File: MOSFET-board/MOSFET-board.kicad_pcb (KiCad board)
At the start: 2 copper layers, 63.5 x 63.5 mm, 104 parts, among them J1 PCIE-LP-01-01-F-DV-A-TR, J2 DB25_Female, U1 BTS3080EJXUMA1, U10 BTS3080EJXUMA1, U11 PCF8575_Breakout, U2 BTS3080EJXUMA1, U3 BTS3080EJXUMA1, U4 BTS3080EJXUMA1, U5 BTS3080EJXUMA1, U6 BTS3080EJXUMA1, U7 BTS3080EJXUMA1, U8 BTS3080EJXUMA1, U9 BTS3080EJXUMA1

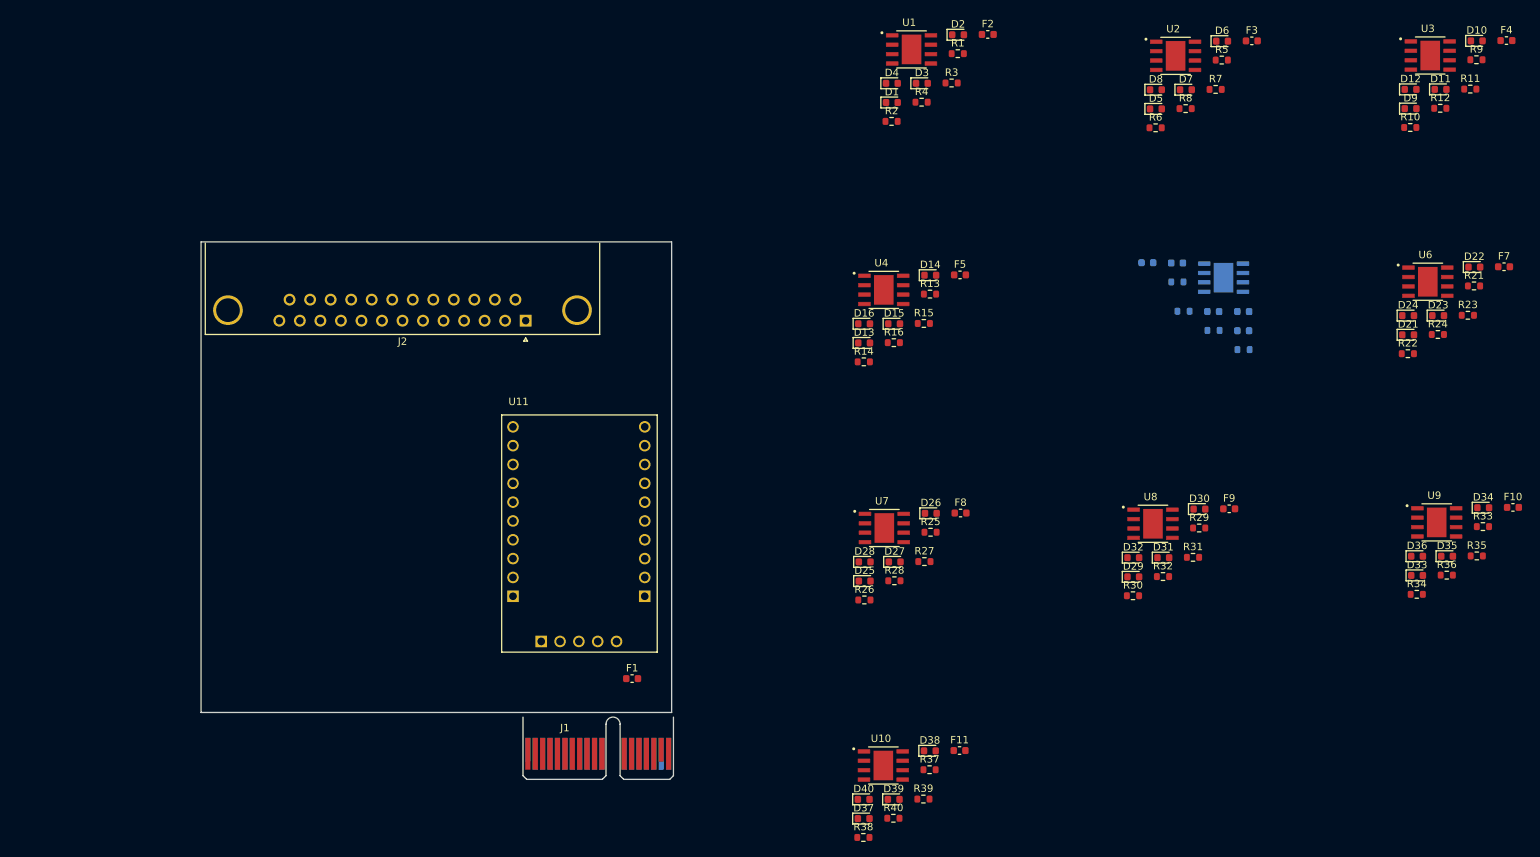
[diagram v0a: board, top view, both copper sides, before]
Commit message: Basic routing for MOSFET board. Need silkscreen update.
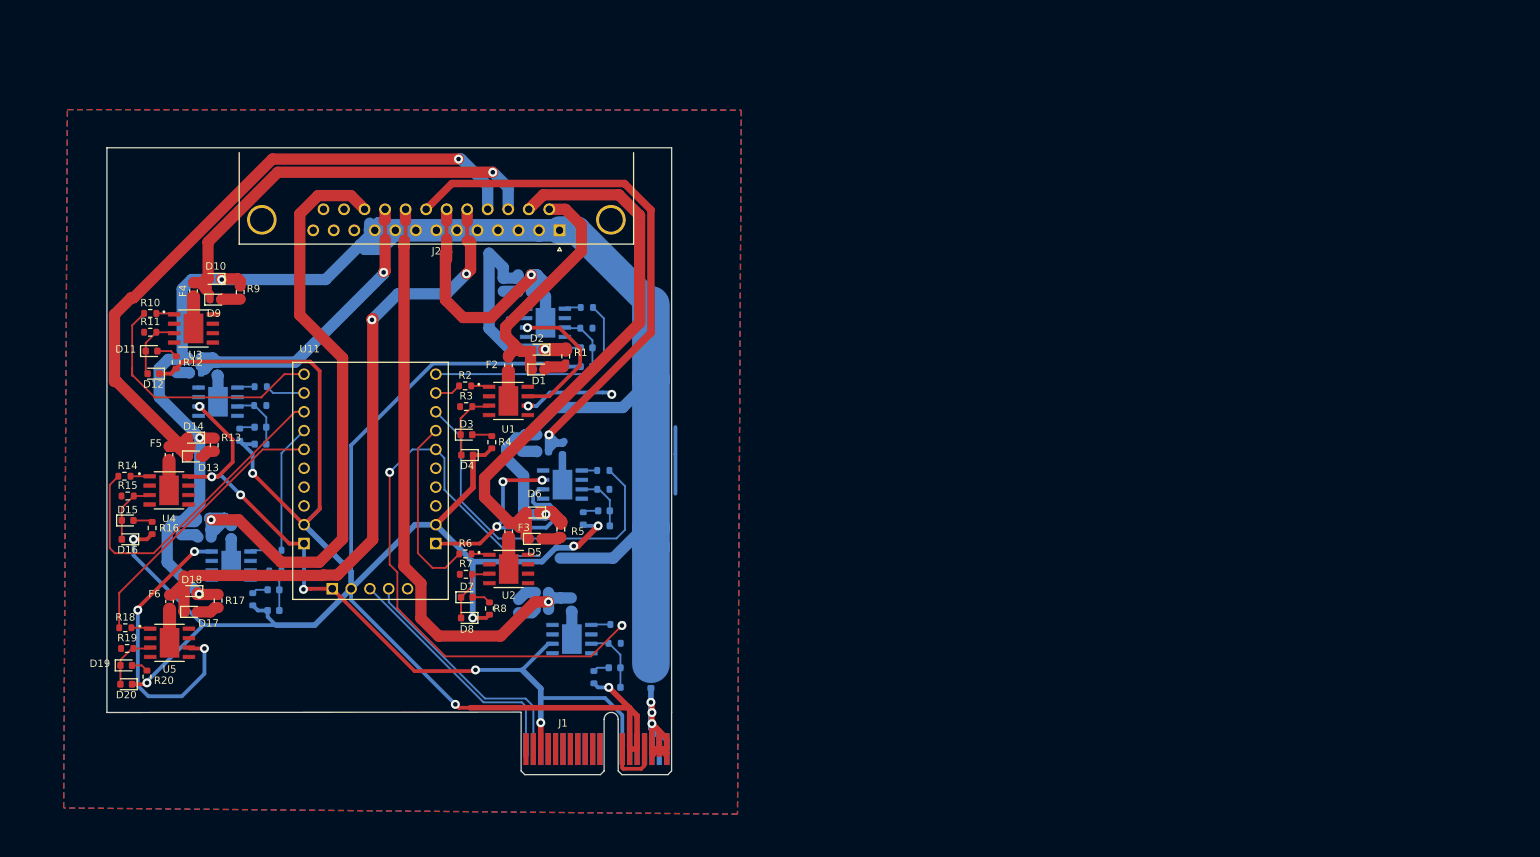
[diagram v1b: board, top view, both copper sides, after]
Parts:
- D17, D18, D19, D20, F6, R17, R18, R19, R20, U5: moved to F.Cu
- D21, D22, D23, D24, D25, D26, D27, D28, D29, D30, D31, D32, D33, D34, D35, D36, D37, D38, D39, D40, F1, F10, F11, F7, F8, F9, R21, R22, R23, R24, R25, R26, R27, R28, R29, R30, R31, R32, R33, R34, R35, R36, R37, R38, R39, R40, U10, U6, U7, U8, U9: moved to B.Cu
- moved R11 181.1 mm to (132.8, 88.4)
- moved F4 180.4 mm to (138.7, 82.8), turned to 90 degrees
- moved R33 177.6 mm to (136.4, 92.9), turned to -90 degrees
- moved D11 177.5 mm to (133.0, 90.9)
- moved F10 175.9 mm to (141.8, 93.2), turned to 90 degrees
- moved D34 175.0 mm to (138.9, 91.9)
- moved R12 174.0 mm to (136.3, 92.5), turned to -90 degrees
- moved D12 173.9 mm to (133.3, 94.0), turned to 180 degrees
- moved D10 173.4 mm to (141.4, 81.2), turned to 180 degrees
- moved R10 171.9 mm to (132.8, 85.9)
- moved U3 170.9 mm to (138.7, 87.9)
- moved R9 169.7 mm to (145.0, 83.0), turned to -90 degrees
- moved D33 167.1 mm to (138.9, 93.9), turned to 180 degrees
- moved R35 165.4 mm to (147.7, 98.3), turned to 180 degrees
- moved U9 165.3 mm to (142.0, 97.8), turned to 180 degrees
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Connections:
- D10 pad 1: Net-(D10-Pad1) -> +12V
- D12 pad 2: PYRO3ST -> Net-(D11-Pad1)
- D14 pad 1: Net-(D14-Pad1) -> +12V
- D16 pad 2: PYRO4ST -> Net-(D15-Pad1)
- D18 pad 1: Net-(D18-Pad1) -> +12V
- D2 pad 1: Net-(D2-Pad1) -> +12V
- D20 pad 2: PYRO5ST -> Net-(D19-Pad1)
- D22 pad 1: Net-(D22-Pad1) -> +12V
- D24 pad 2: PYRO6ST -> Net-(D23-Pad1)
- D26 pad 1: Net-(D26-Pad1) -> +12V
- D28 pad 2: PYRO7ST -> Net-(D27-Pad1)
- D30 pad 1: Net-(D30-Pad1) -> +12V
- D32 pad 2: PYRO8ST -> Net-(D31-Pad1)
- D34 pad 1: Net-(D34-Pad1) -> +12V
- D36 pad 2: PYRO9ST -> Net-(D35-Pad1)
- D38 pad 1: Net-(D38-Pad1) -> +12V
- D4 pad 2: PYRO1ST -> Net-(D3-Pad1)
- D40 pad 2: PYRO10ST -> Net-(D39-Pad1)
- D6 pad 1: Net-(D6-Pad1) -> +12V
- D8 pad 2: PYRO2ST -> Net-(D7-Pad1)
- F10 pad 1: +12V -> Net-(F10-Pad1)
- F10 pad 2: Net-(D34-Pad1) -> PYRO9
- F11 pad 1: +12V -> Net-(F11-Pad1)
- F11 pad 2: Net-(D38-Pad1) -> PYRO10
- F2 pad 1: +12V -> Net-(F2-Pad1)
- F2 pad 2: Net-(D2-Pad1) -> PYRO1
- F3 pad 1: +12V -> Net-(F3-Pad1)
- F3 pad 2: Net-(D6-Pad1) -> PYRO2
- F4 pad 1: +12V -> Net-(F4-Pad1)
- F4 pad 2: Net-(D10-Pad1) -> PYRO3
- F5 pad 1: +12V -> Net-(F5-Pad1)
- F5 pad 2: Net-(D14-Pad1) -> PYRO4
- F6 pad 1: +12V -> Net-(F6-Pad1)
- F6 pad 2: Net-(D18-Pad1) -> PYRO5
- F7 pad 1: +12V -> Net-(F7-Pad1)
- F7 pad 2: Net-(D22-Pad1) -> PYRO6
- F8 pad 1: +12V -> Net-(F8-Pad1)
- F8 pad 2: Net-(D26-Pad1) -> PYRO7
- F9 pad 1: +12V -> Net-(F9-Pad1)
- F9 pad 2: Net-(D30-Pad1) -> PYRO8
- R1 pad 1: Net-(D2-Pad1) -> +12V
- R11 pad 1: PYRO3ST -> /Pyro 3/Status
- R13 pad 1: Net-(D14-Pad1) -> +12V
- R15 pad 1: PYRO4ST -> /Pyro 4/Status
- R17 pad 1: Net-(D18-Pad1) -> +12V
- R19 pad 1: PYRO5ST -> /Pyro 5/Status
- R21 pad 1: Net-(D22-Pad1) -> +12V
- R23 pad 1: PYRO6ST -> /Pyro 6/Status
- R25 pad 1: Net-(D26-Pad1) -> +12V
- R27 pad 1: PYRO7ST -> /Pyro 7/Status
- R29 pad 1: Net-(D30-Pad1) -> +12V
- R3 pad 1: PYRO1ST -> /Pyro 1/Status
- R31 pad 1: PYRO8ST -> /Pyro 8/Status
- R33 pad 1: Net-(D34-Pad1) -> +12V
- R35 pad 1: PYRO9ST -> /Pyro 9/Status
- R37 pad 1: Net-(D38-Pad1) -> +12V
- R39 pad 1: PYRO10ST -> /Pyro 10/Status
- R5 pad 1: Net-(D6-Pad1) -> +12V
- R7 pad 1: PYRO2ST -> /Pyro 2/Status
- R9 pad 1: Net-(D10-Pad1) -> +12V
- U1 pad 9: PYRO1 -> Net-(F2-Pad1)
- U10 pad 9: PYRO10 -> Net-(F11-Pad1)
- U11 pad 1: PYRO9EN -> PYRO3EN
- U11 pad 18: PYRO1EN -> unconnected-(U11-Pad18)
- U11 pad 19: PYRO2EN -> unconnected-(U11-Pad19)
- U11 pad 2: PYRO10EN -> PYRO9EN
- U11 pad 20: PYRO3EN -> unconnected-(U11-Pad20)
- U11 pad 21: PYRO4EN -> PYRO8EN
- U11 pad 22: PYRO5EN -> PYRO2EN
- U11 pad 23: PYRO6EN -> PYRO7EN
- U11 pad 24: PYRO7EN -> PYRO1EN
- U11 pad 25: PYRO8EN -> PYRO6EN
- U11 pad 3: unconnected-(U11-Pad3) -> PYRO4EN
- U11 pad 4: unconnected-(U11-Pad4) -> PYRO10EN
- U11 pad 5: unconnected-(U11-Pad5) -> PYRO5EN
- U2 pad 9: PYRO2 -> Net-(F3-Pad1)
- U3 pad 9: PYRO3 -> Net-(F4-Pad1)
- U4 pad 9: PYRO4 -> Net-(F5-Pad1)
- U5 pad 9: PYRO5 -> Net-(F6-Pad1)
- U6 pad 9: PYRO6 -> Net-(F7-Pad1)
- U7 pad 9: PYRO7 -> Net-(F8-Pad1)
- U8 pad 9: PYRO8 -> Net-(F9-Pad1)
- U9 pad 9: PYRO9 -> Net-(F10-Pad1)
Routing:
- net +3.3V: track 0.00 -> 320.8 mm, vias 0 -> 8
- net +12V: track 0.00 -> 283.2 mm, vias 0 -> 5
- net GND: track 0.00 -> 223.7 mm, vias 0 -> 15
- net PYRO4: track 0.00 -> 92.8 mm, vias 0 -> 1
- net PYRO5: track 0.00 -> 90.0 mm, vias 0 -> 2
- net PYRO10: track 0.00 -> 86.8 mm, vias 0 -> 1
- net PYRO8: track 0.00 -> 83.9 mm, vias 0 -> 1
- net PYRO8EN: track 0.00 -> 83.7 mm, vias 0 -> 2
- net PYRO2: track 0.00 -> 76.2 mm
- net PYRO7: track 0.00 -> 75.7 mm, vias 0 -> 1
- net PYRO3: track 0.00 -> 59.5 mm, vias 0 -> 1
- net PYRO7EN: track 0.00 -> 47.0 mm
- net PYRO9: track 0.00 -> 44.7 mm, vias 0 -> 1
- net PYRO4EN: track 0.00 -> 44.6 mm
- net PYRO6: track 0.00 -> 39.6 mm, vias 0 -> 1
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- added copper zone on B.Cu, net GND
- added copper zone on F.Cu, net GND
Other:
- board size 63.5 x 63.5 mm -> 76.2 x 76.2 mm

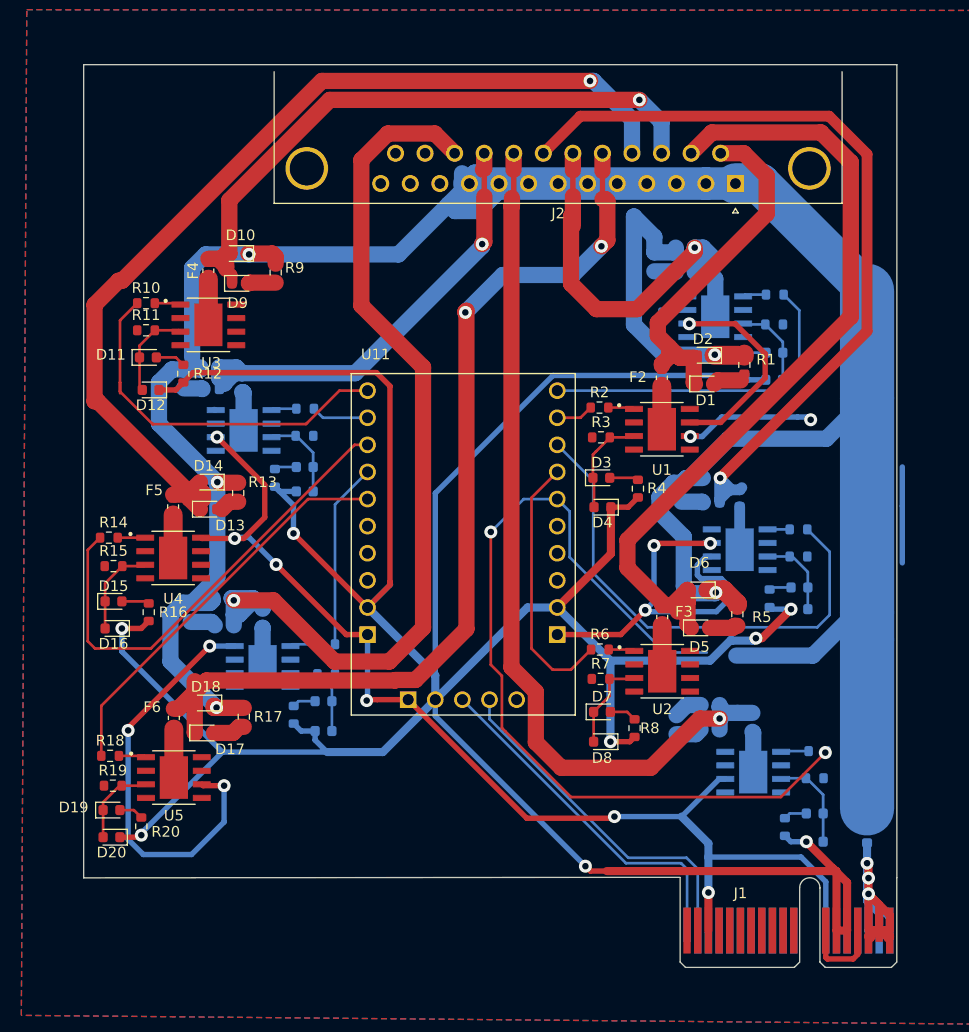
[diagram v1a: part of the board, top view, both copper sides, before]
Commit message: updates for layout MOSFET/HX
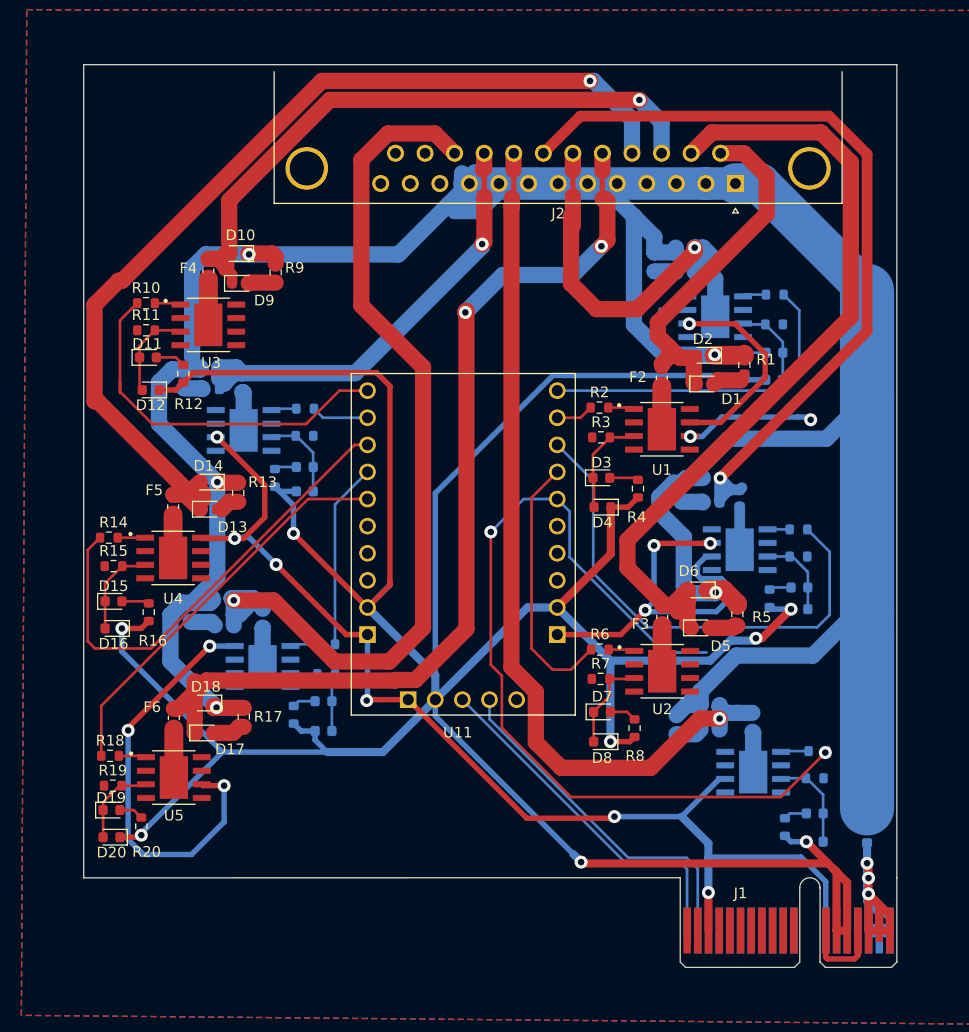
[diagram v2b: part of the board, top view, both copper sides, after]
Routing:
- net +12V: track 283.2 -> 296.7 mm
- net (no net): track 8.99 -> 0.00 mm
- net GND: track 223.7 -> 226.0 mm
- net +3.3V: track 320.8 -> 319.8 mm
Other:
- outline, holes or cut-outs redrawn
